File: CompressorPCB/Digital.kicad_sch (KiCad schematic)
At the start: 22 parts, among them J2 SWD Header, SW2 RST, U6 NCS20074D, U7 STM32L052K6T6

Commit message: digital side schematic stuff
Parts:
- added C18: 100n, symbol Device:C
- added D10, D9: BAT54S, Package_TO_SOT_SMD:SOT-23, symbol Diode:BAT54S
- added R53, R54: 4k7, symbol Device:R_US
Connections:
- net +18V: now also C18.1
- net +3.3VA: now also D10.2 (K), D9.2 (K)
- net GND: now also C18.2, D10.1 (A), D9.1 (A)
- net LED_Latch: now reaches U7.10 (PA4)
- net LED_SCK: now reaches U7.11 (PA5)
- net LED_MOSI: now reaches U7.13 (PA7)
- net LED_NRST: now reaches U7.14 (PB0)
- net Control_ADC: now reaches U7.7 (PA1)
- net Control_ADC: now also D9.3 (COM), R53.2
- net Output_ADC: now reaches U7.8 (PA2)
- net Output_ADC: now also D10.3 (COM), R54.2
- net Env renamed ENV
- net EnvOut: no longer names the net of R46.2, U6.8
- net EnvOut: now also R53.1
- net SigOut renamed OUT_BIASED
- net VG renamed +9VA
- net VUout: no longer names the net of R50.2, U6.14
- net VUout: now also R54.1
- no-connect marks 22 -> 16
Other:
- moved on the sheet: R49, R50, U6B, U6D, U6E

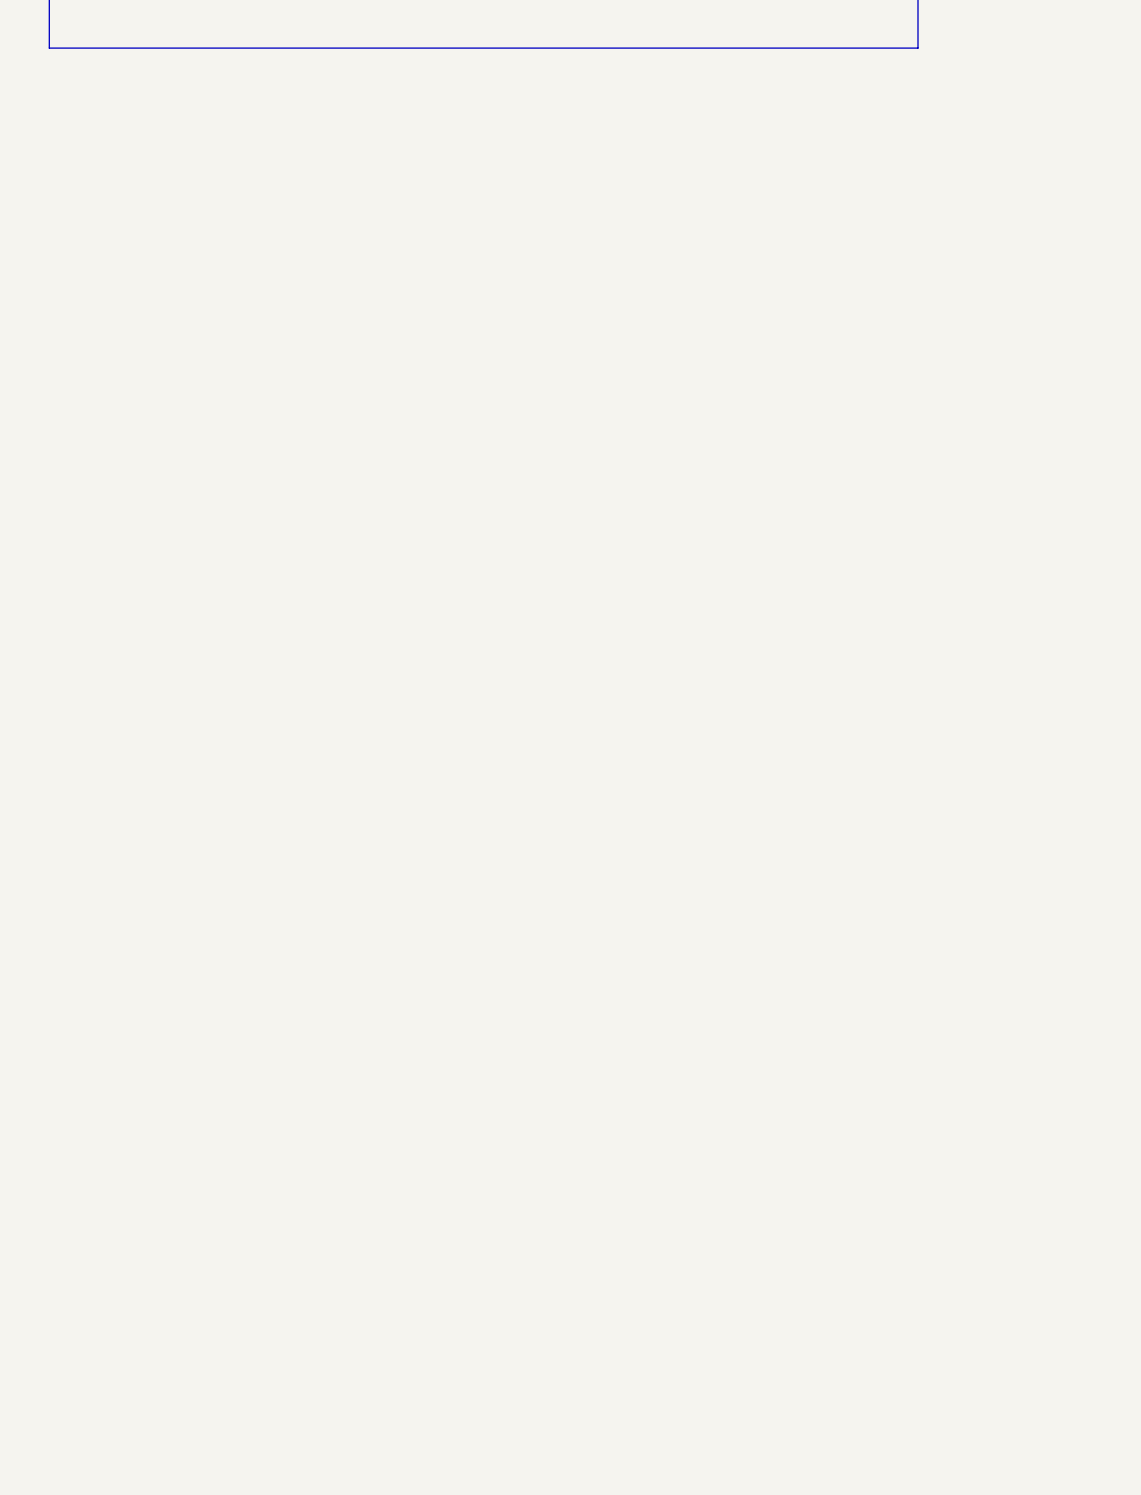
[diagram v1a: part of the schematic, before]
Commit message: shift register LED driver
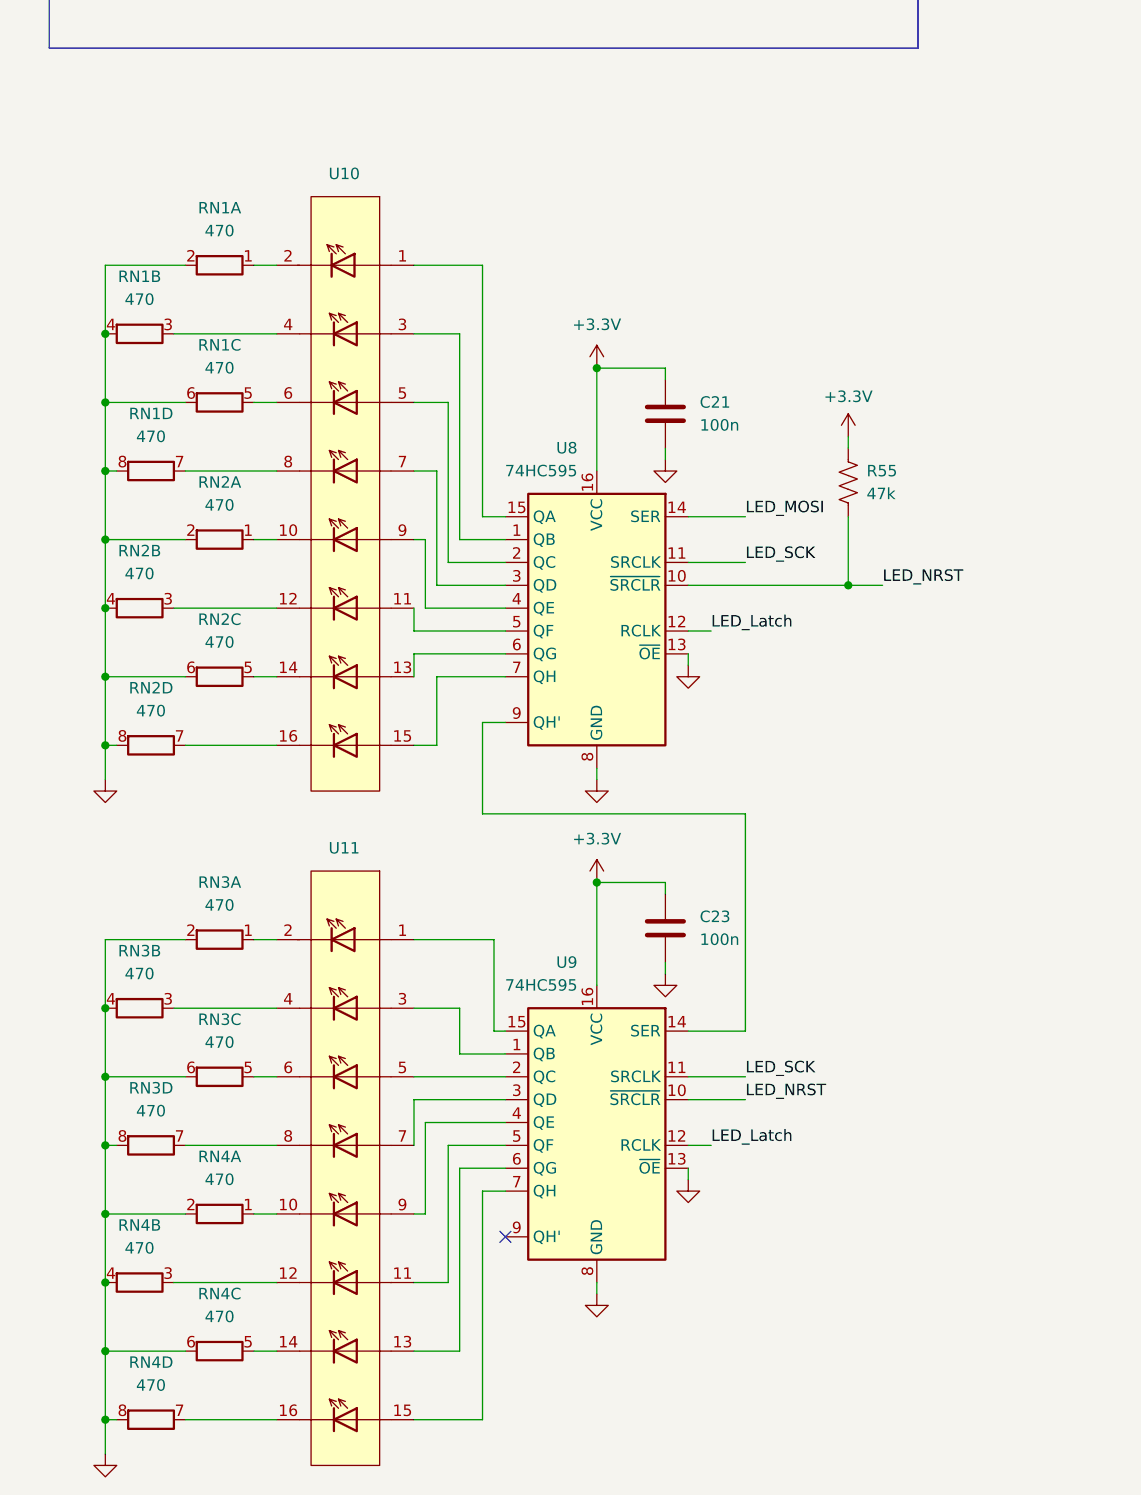
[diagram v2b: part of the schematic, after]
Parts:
- added C21, C23: 100n, symbol Device:C
- added R55: 47k, Resistor_SMD:R_0805_2012Metric, symbol Device:R_US
- added RN1, RN2, RN3, RN4: 470, Resistor_THT:R_Array_SIP8, symbol Device:R_Pack04_SIP_Split
- added U10, U11: (no value), symbol LED:OctoLED_0805
- added U8, U9: 74HC595, Package_SO:SOIC-16_3.9x9.9mm_P1.27mm, symbol 74xx:74HC595
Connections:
- net +3.3V: now also C21.1, C23.1, R55.1, U8.16 (VCC), U9.16 (VCC)
- net GND: now also C21.2, C23.2, RN1.2 (R1.2), RN1.4 (R2.2), RN1.6 (R3.2), RN1.8 (R4.2), RN2.2 (R1.2), RN2.4 (R2.2), RN2.6 (R3.2), RN2.8 (R4.2), RN3.2 (R1.2), RN3.4 (R2.2), RN3.6 (R3.2), RN3.8 (R4.2), RN4.2 (R1.2), RN4.4 (R2.2), RN4.6 (R3.2), RN4.8 (R4.2), U8.13 (~{OE}), U8.8 (GND), U9.13 (~{OE}), U9.8 (GND)
- net LED_Latch: now also U8.12 (RCLK), U9.12 (RCLK)
- net LED_MOSI: now also U8.14 (SER)
- net LED_NRST: now also R55.2, U8.10 (~{SRCLR}), U9.10 (~{SRCLR})
- net LED_SCK: now also U8.11 (SRCLK), U9.11 (SRCLK)
- new net: RN3.7 (R4.1), U11.8 (2)
- new net: RN3.3 (R2.1), U11.4 (2)
- new net: RN3.1 (R1.1), U11.2
- new net: RN4.7 (R4.1), U11.16 (2)
- new net: RN3.5 (R3.1), U11.6 (2)
- new net: RN1.3 (R2.1), U10.4 (2)
- new net: RN2.5 (R3.1), U10.14 (2)
- new net: U11.1, U9.15 (QA)
- new net: RN4.1 (R1.1), U11.10 (2)
- new net: U11.11 (1), U9.5 (QF)
- new net: RN4.3 (R2.1), U11.12 (2)
- new net: U11.13 (1), U9.6 (QG)
- new net: RN4.5 (R3.1), U11.14 (2)
- new net: U11.15 (1), U9.7 (QH)
- new net: U11.3 (1), U9.1 (QB)
- new net: U11.5 (1), U9.2 (QC)
- new net: U11.7 (1), U9.3 (QD)
- new net: U11.9 (1), U9.4 (QE)
- new net: RN1.7 (R4.1), U10.8 (2)
- new net: RN2.7 (R4.1), U10.16 (2)
- new net: RN2.3 (R2.1), U10.12 (2)
- new net: RN2.1 (R1.1), U10.10 (2)
- new net: U8.9 (QH'), U9.14 (SER)
- new net: RN1.5 (R3.1), U10.6 (2)
- new net: U10.1, U8.15 (QA)
- new net: U10.11 (1), U8.5 (QF)
- new net: U10.13 (1), U8.6 (QG)
- new net: U10.15 (1), U8.7 (QH)
- new net: RN1.1 (R1.1), U10.2
- new net: U10.3 (1), U8.1 (QB)
- new net: U10.5 (1), U8.2 (QC)
- new net: U10.7 (1), U8.3 (QD)
- new net: U10.9 (1), U8.4 (QE)
- no-connect marks 16 -> 17

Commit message: schematic labels, footprints chosen
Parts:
- removed D7, D8: D, symbol Simulation_SPICE:D
- added D1, D2: 1N4148W, Diode_SMD:D_SOD-123, symbol Diode:1N4148W
- added D11: Orange, LED_THT:LED_D3.0mm, symbol Device:LED
- added J3: Header, Connector_PinHeader_2.54mm:PinHeader_1x06_P2.54mm_Vertical, symbol Connector:Conn_01x06_Pin
- added J5: In, Connector_Audio:Jack_6.35mm_Tayda_PJ664C_Mono_Horizontal, symbol Connector_Audio:AudioJack2_Switch
- added J6: Out, Connector_Audio:Jack_6.35mm_Tayda_PJ664C_Mono_Horizontal, symbol Connector_Audio:AudioJack2_Switch
- added J8: (no value), Connector:BatteryContact_Keystone_243, symbol Connector:GroundingSpring
- added Q4: 2N7002, Package_TO_SOT_SMD:SOT-23, symbol Transistor_FET:2N7002
- added R56: 47k, Resistor_SMD:R_0805_2012Metric, symbol Device:R_US
- added R57: 470, Resistor_SMD:R_0805_2012Metric, symbol Device:R_US
- C16, C18, C21, C23: footprint (none) -> Capacitor_SMD:C_0805_2012Metric
- R42, R43, R44, R45, R46, R47, R48, R49, R50, R53, R54: footprint (none) -> Resistor_SMD:R_0805_2012Metric
- U10, U11: footprint (none) -> LED_SMD:LED_OctoLED_0805
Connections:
- net +3.3V: now also R56.1, R57.1
- net BYP_IN: now also J3.5 (Pin_5), R56.2
- net GND: now also J3.6 (Pin_6), J5.S, J5.SN, J6.S, J6.SN, J8.1, Q4.2 (S)
- net Rect: now also D1.1 (K)
- net at U6.1: now also D1.2 (A), D2.1 (K)
- net at R42.1, R47.2, U6.2 (-): now also D2.2 (A)
- net BYP_LED: now reaches U7.26 (PB3)
- net BYP_LED: now also Q4.1 (G)
- new net: D11.1 (K), Q4.3 (D)
- new net: D11.2 (A), R57.2
- new net FX_IN: J3.2 (Pin_2)
- new net FX_OUT: J3.4 (Pin_4)
- new net InJack: J3.1 (Pin_1), J5.T
- new net OutJack: J3.3 (Pin_3), J6.T
- no-connect marks 17 -> 18
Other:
- note added: "ADC input stage"
- note added: "Jacks and headers"
- note added: "RASR LED driver"
- moved on the sheet: C16, C18, C21, C23, D10, D9, J2, R42, R43, R44, R45, R46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

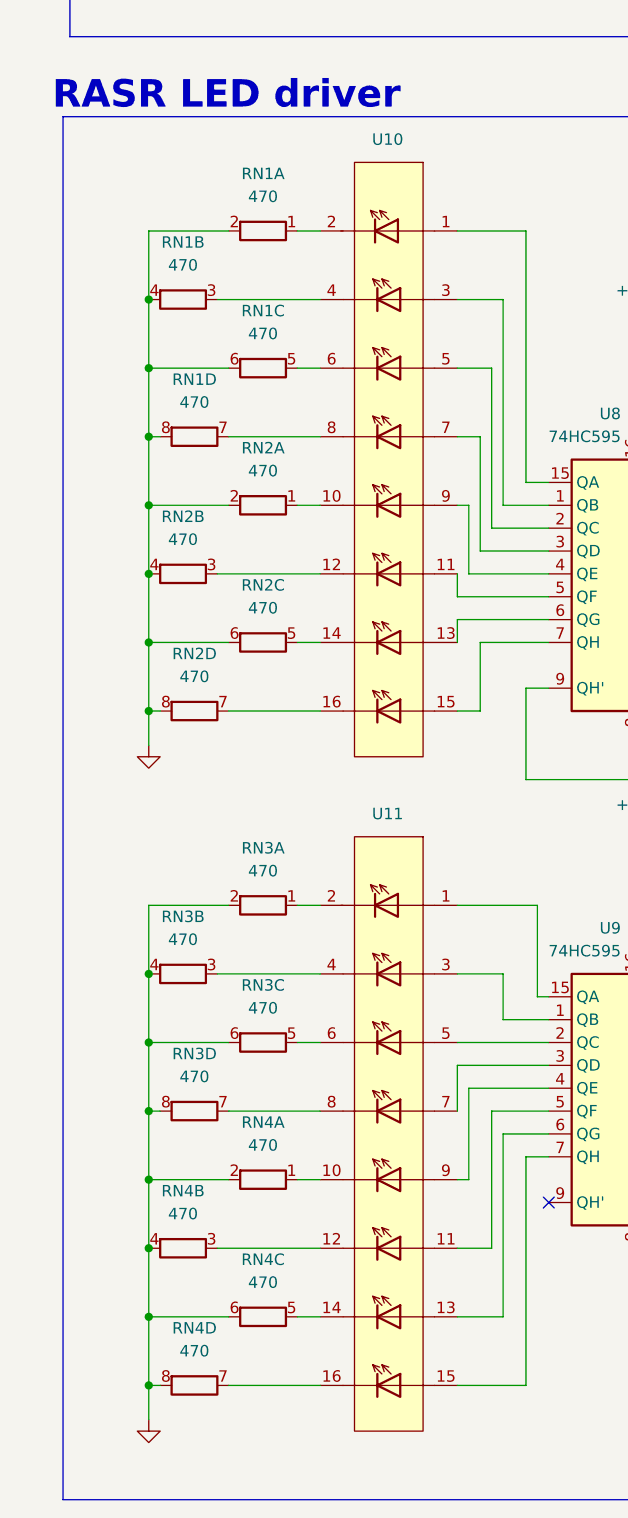
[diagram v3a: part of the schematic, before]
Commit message: fixed resistor array footprints
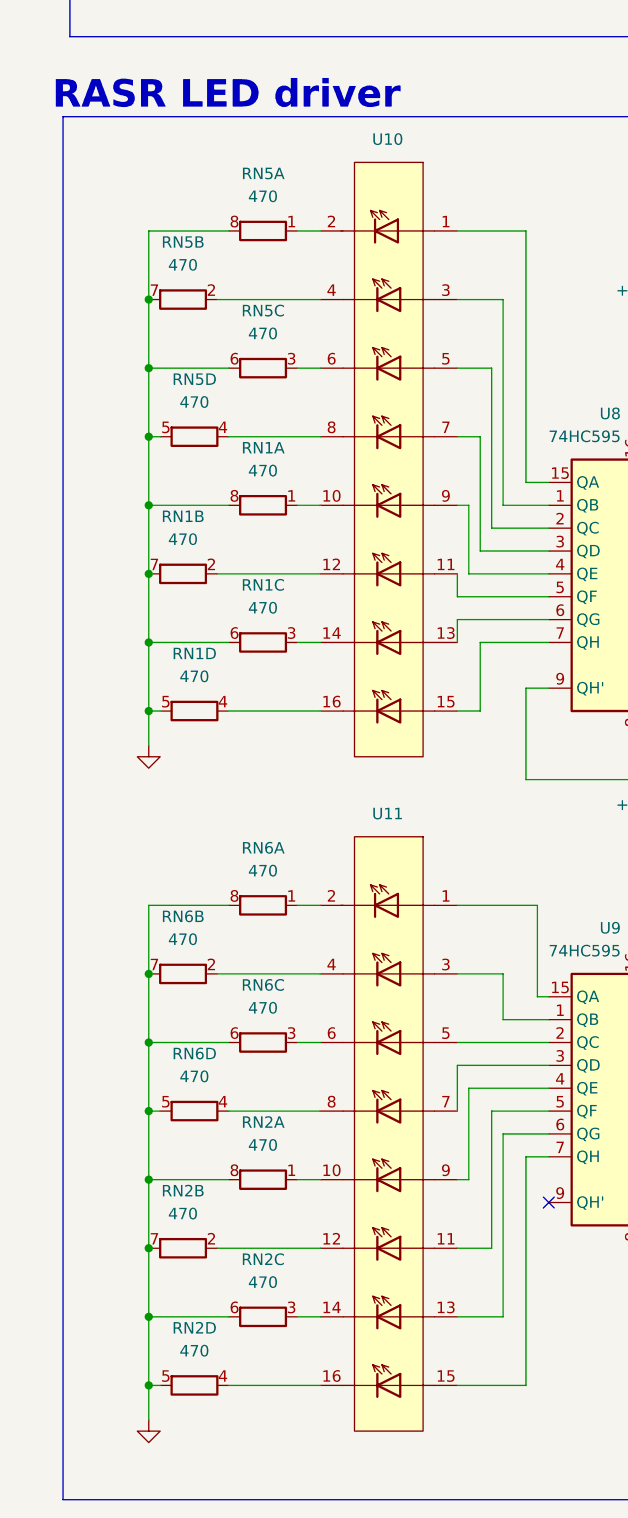
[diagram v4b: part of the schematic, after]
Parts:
- removed RN1, RN2, RN3, RN4: 470, Resistor_THT:R_Array_SIP8, symbol Device:R_Pack04_SIP_Split
- added RN1, RN2, RN5, RN6: 470, Resistor_SMD:R_Cat16-4, symbol Device:R_Pack04_Split
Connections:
- net GND: now also RN1.5 (R4.2), RN1.6 (R3.2), RN1.7 (R2.2), RN1.8 (R1.2), RN2.5 (R4.2), RN2.6 (R3.2), RN2.7 (R2.2), RN2.8 (R1.2), RN5.5 (R4.2), RN5.6 (R3.2), RN5.7 (R2.2), RN5.8 (R1.2), RN6.5 (R4.2), RN6.6 (R3.2), RN6.7 (R2.2), RN6.8 (R1.2)
- net at U11.8 (2): now also RN6.4 (R4.1)
- net at U11.4 (2): now also RN6.2 (R2.1)
- net at U11.2: now also RN6.1 (R1.1)
- net at U11.16 (2): now also RN2.4 (R4.1)
- net at U11.6 (2): now also RN6.3 (R3.1)
- net at U10.4 (2): now also RN5.2 (R2.1)
- net at U10.14 (2): now also RN1.3 (R3.1)
- net at U11.10 (2): now also RN2.1 (R1.1)
- net at U11.12 (2): now also RN2.2 (R2.1)
- net at U11.14 (2): now also RN2.3 (R3.1)
- net at U10.8 (2): now also RN5.4 (R4.1)
- net at U10.16 (2): now also RN1.4 (R4.1)
- net at U10.12 (2): now also RN1.2 (R2.1)
- net at U10.10 (2): now also RN1.1 (R1.1)
- net at U10.6 (2): now also RN5.3 (R3.1)
- net at U10.2: now also RN5.1 (R1.1)

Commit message: basic layout
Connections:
- net BYP_LED: now also U7.20 (PA10); no longer U7.26 (PB3)
- net GND: now also RN1.1 (R1.1), RN1.2 (R2.1), RN1.3 (R3.1), RN1.4 (R4.1), RN2.1 (R1.1), RN2.2 (R2.1), RN2.3 (R3.1), RN2.4 (R4.1), RN5.1 (R1.1), RN5.2 (R2.1), RN5.3 (R3.1), RN5.4 (R4.1), RN6.1 (R1.1), RN6.2 (R2.1), RN6.3 (R3.1), RN6.4 (R4.1); no longer RN1.5 (R4.2), RN1.6 (R3.2), RN1.7 (R2.2), RN1.8 (R1.2), RN2.5 (R4.2), RN2.6 (R3.2), RN2.7 (R2.2), RN2.8 (R1.2), RN5.5 (R4.2), RN5.6 (R3.2), RN5.7 (R2.2), RN5.8 (R1.2), RN6.5 (R4.2), RN6.6 (R3.2), RN6.7 (R2.2), RN6.8 (R1.2)
- net LED_Latch: now also U7.25 (PA15); no longer U7.10 (PA4)
- net LED_MOSI: now also U7.28 (PB5); no longer U7.13 (PA7)
- net LED_NRST: now also U7.29 (PB6); no longer U7.14 (PB0)
- net LED_SCK: now also U7.26 (PB3); no longer U7.11 (PA5)
- net at U11.8 (2): now also RN6.5 (R4.2); no longer RN6.4 (R4.1)
- net at R46.2, R53.1: now also U6.14; no longer U6.8
- net at U11.10 (2): now also RN2.8 (R1.2); no longer RN2.1 (R1.1)
- net at U10.2: now also RN5.8 (R1.2); no longer RN5.1 (R1.1)
- net at U10.12 (2): now also RN1.7 (R2.2); no longer RN1.2 (R2.1)
- net at U11.16 (2): now also RN2.5 (R4.2); no longer RN2.4 (R4.1)
- net at R44.2, R46.1: now also U6.13 (-); no longer U6.9 (-)
- net at U10.10 (2): now also RN1.8 (R1.2); no longer RN1.1 (R1.1)
- net at U11.4 (2): now also RN6.7 (R2.2); no longer RN6.2 (R2.1)
- net at R49.2, R50.1: now also U6.9 (-); no longer U6.13 (-)
- net at R50.2, R54.1: now also U6.8; no longer U6.14
- net at U11.12 (2): now also RN2.7 (R2.2); no longer RN2.2 (R2.1)
- net at U11.14 (2): now also RN2.6 (R3.2); no longer RN2.3 (R3.1)
- net at U11.2: now also RN6.8 (R1.2); no longer RN6.1 (R1.1)
- net at U11.6 (2): now also RN6.6 (R3.2); no longer RN6.3 (R3.1)
- net at U10.6 (2): now also RN5.6 (R3.2); no longer RN5.3 (R3.1)
- net at U10.4 (2): now also RN5.7 (R2.2); no longer RN5.2 (R2.1)
- net at U10.8 (2): now also RN5.5 (R4.2); no longer RN5.4 (R4.1)
- net at U10.16 (2): now also RN1.5 (R4.2); no longer RN1.4 (R4.1)
- net at U10.14 (2): now also RN1.6 (R3.2); no longer RN1.3 (R3.1)
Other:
- moved on the sheet: C18, RN1A, RN1B, RN1C, RN1D, RN2A, RN2B, RN2C, RN2D, RN5A, RN5B, RN5C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
